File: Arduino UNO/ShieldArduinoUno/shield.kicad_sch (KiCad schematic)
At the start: 10 parts

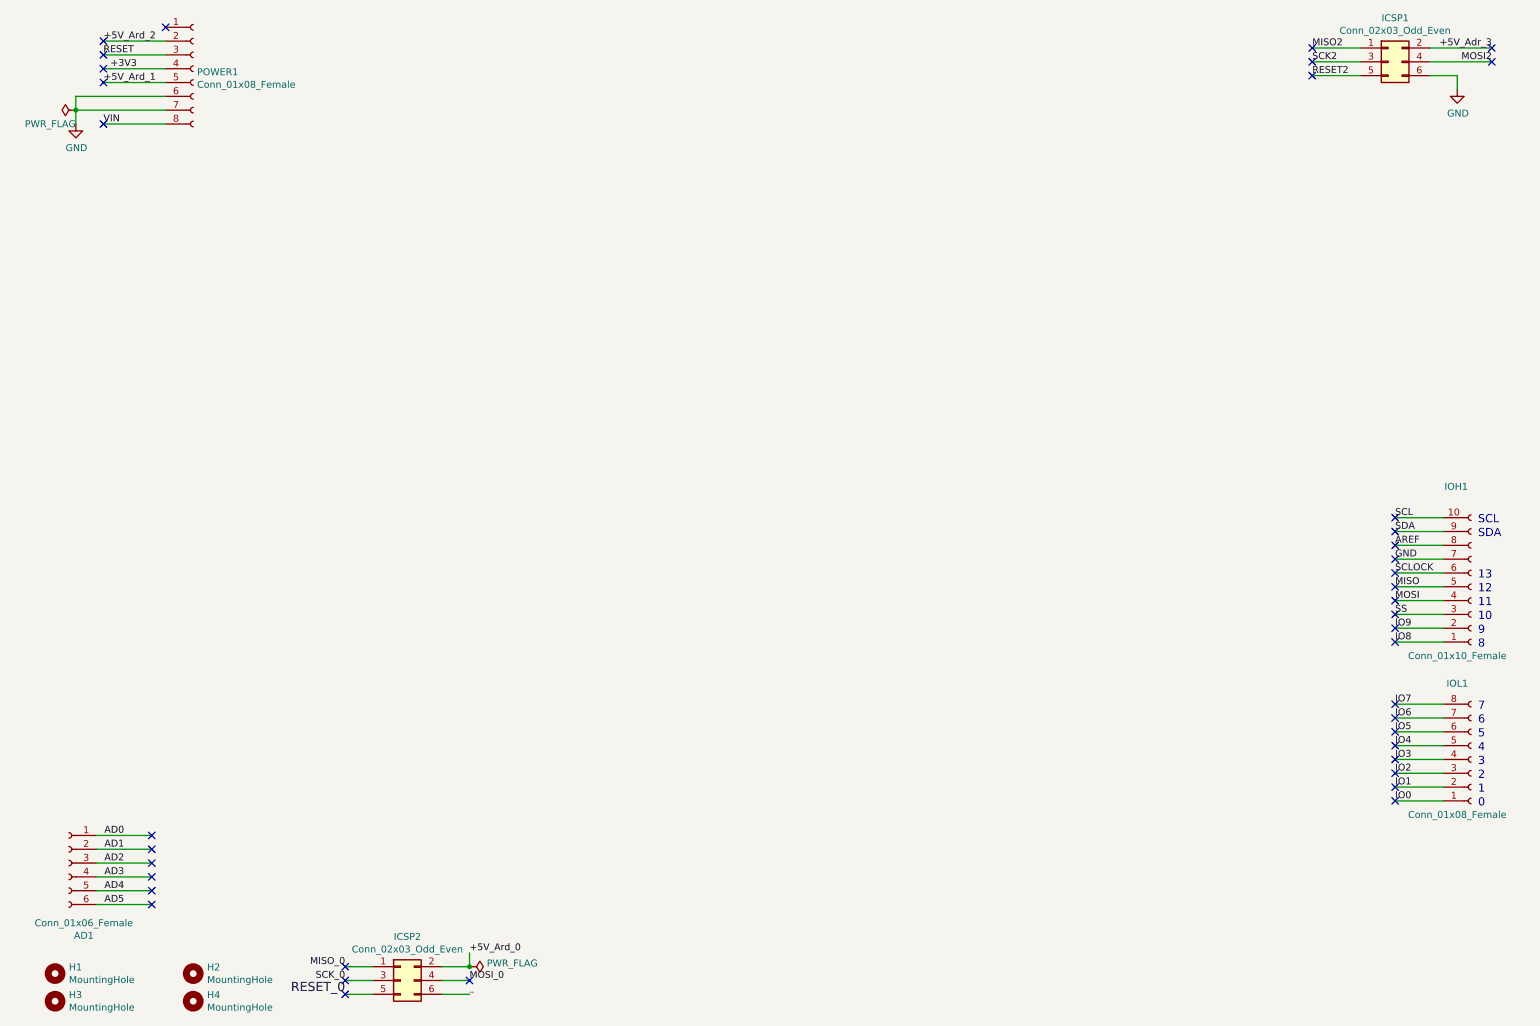
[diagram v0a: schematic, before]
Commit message: Update shield.kicad_pcb, shield.kicad_pro, and shield.kicad_sch to KiCad 7
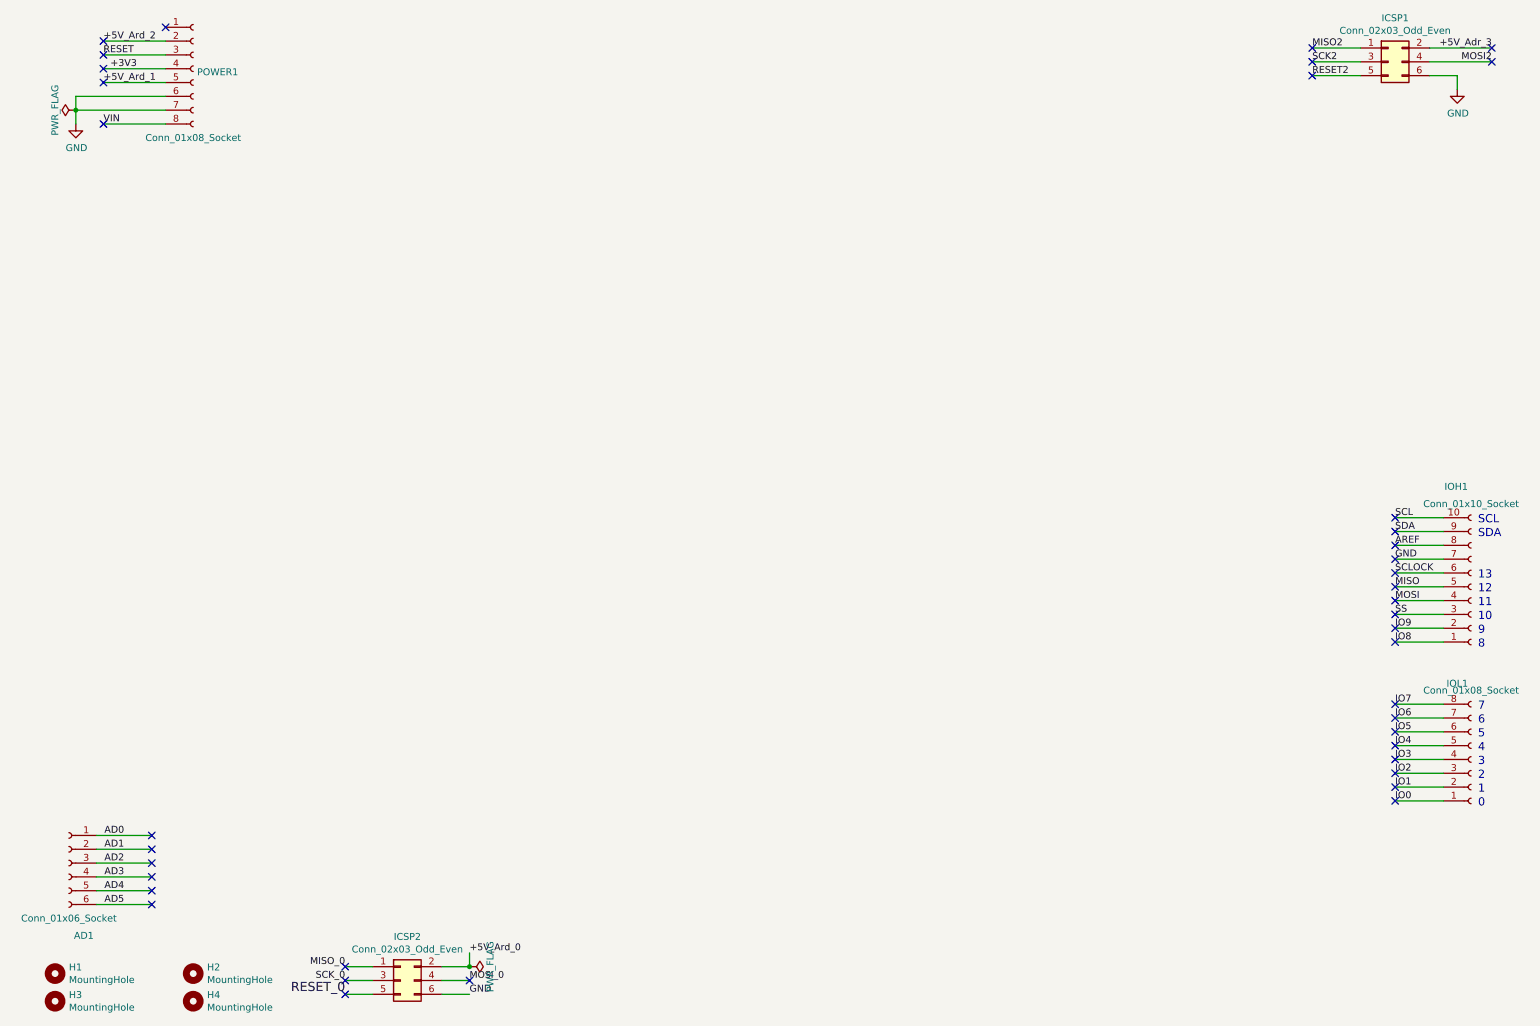
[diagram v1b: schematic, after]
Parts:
- AD1: value Conn_01x06_Female -> Conn_01x06_Socket; symbol Connector:Conn_01x06_Female -> Connector:Conn_01x06_Socket
- IOH1: value Conn_01x10_Female -> Conn_01x10_Socket; symbol Connector:Conn_01x10_Female -> Connector:Conn_01x10_Socket
- IOL1, POWER1: value Conn_01x08_Female -> Conn_01x08_Socket; symbol Connector:Conn_01x08_Female -> Connector:Conn_01x08_Socket

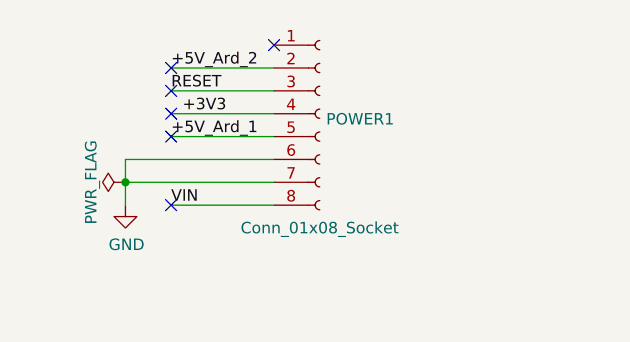
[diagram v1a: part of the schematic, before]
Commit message: REinstated IOREF
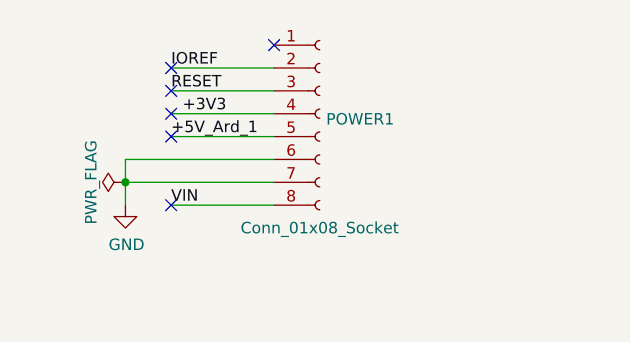
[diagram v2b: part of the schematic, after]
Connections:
- net +5V_Ard_2 renamed IOREF
